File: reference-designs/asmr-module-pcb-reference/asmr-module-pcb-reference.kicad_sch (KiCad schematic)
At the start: 2 parts

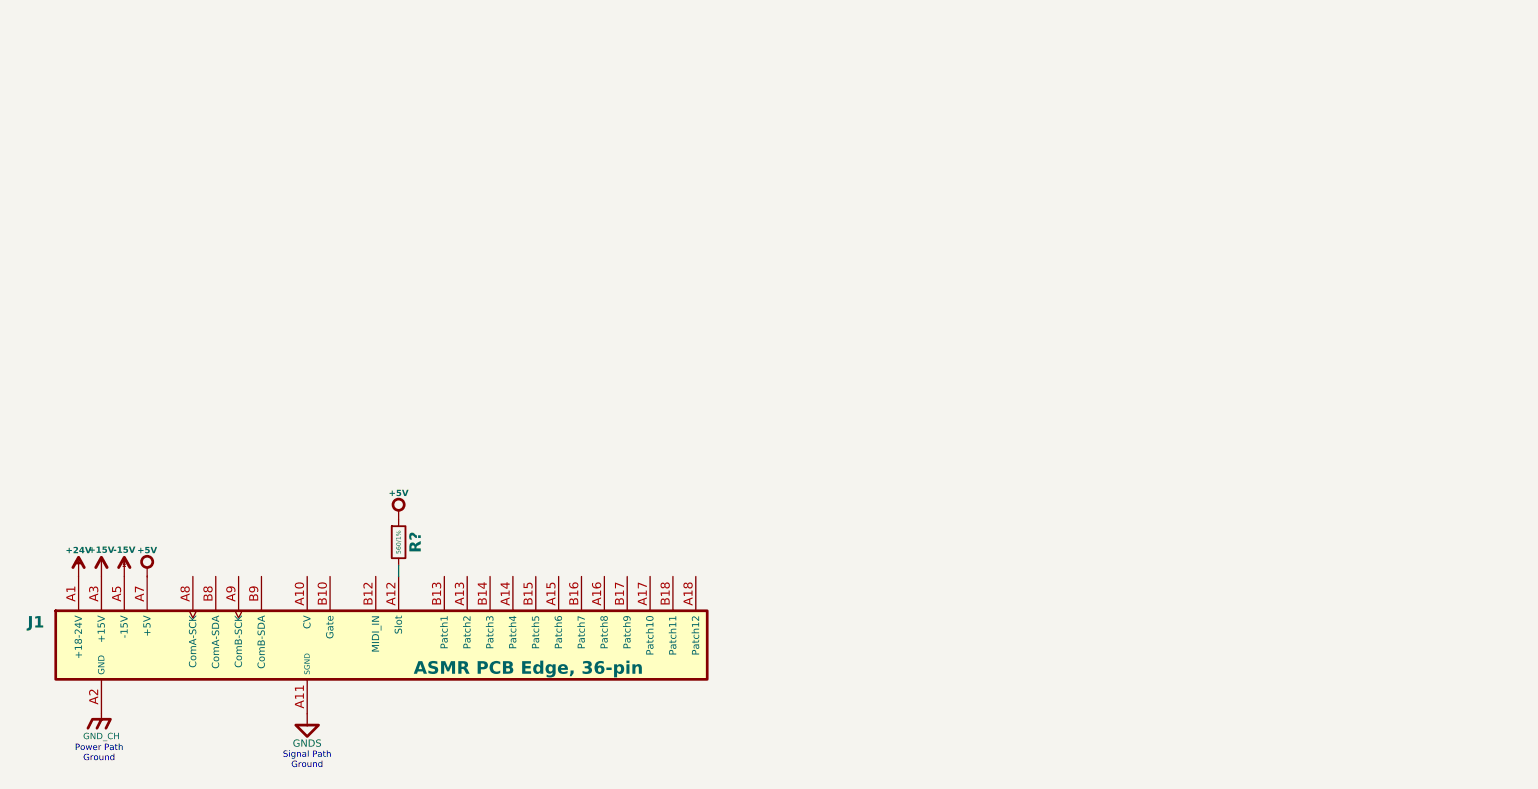
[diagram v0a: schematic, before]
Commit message: Update reference design for 64-pin edge connector.
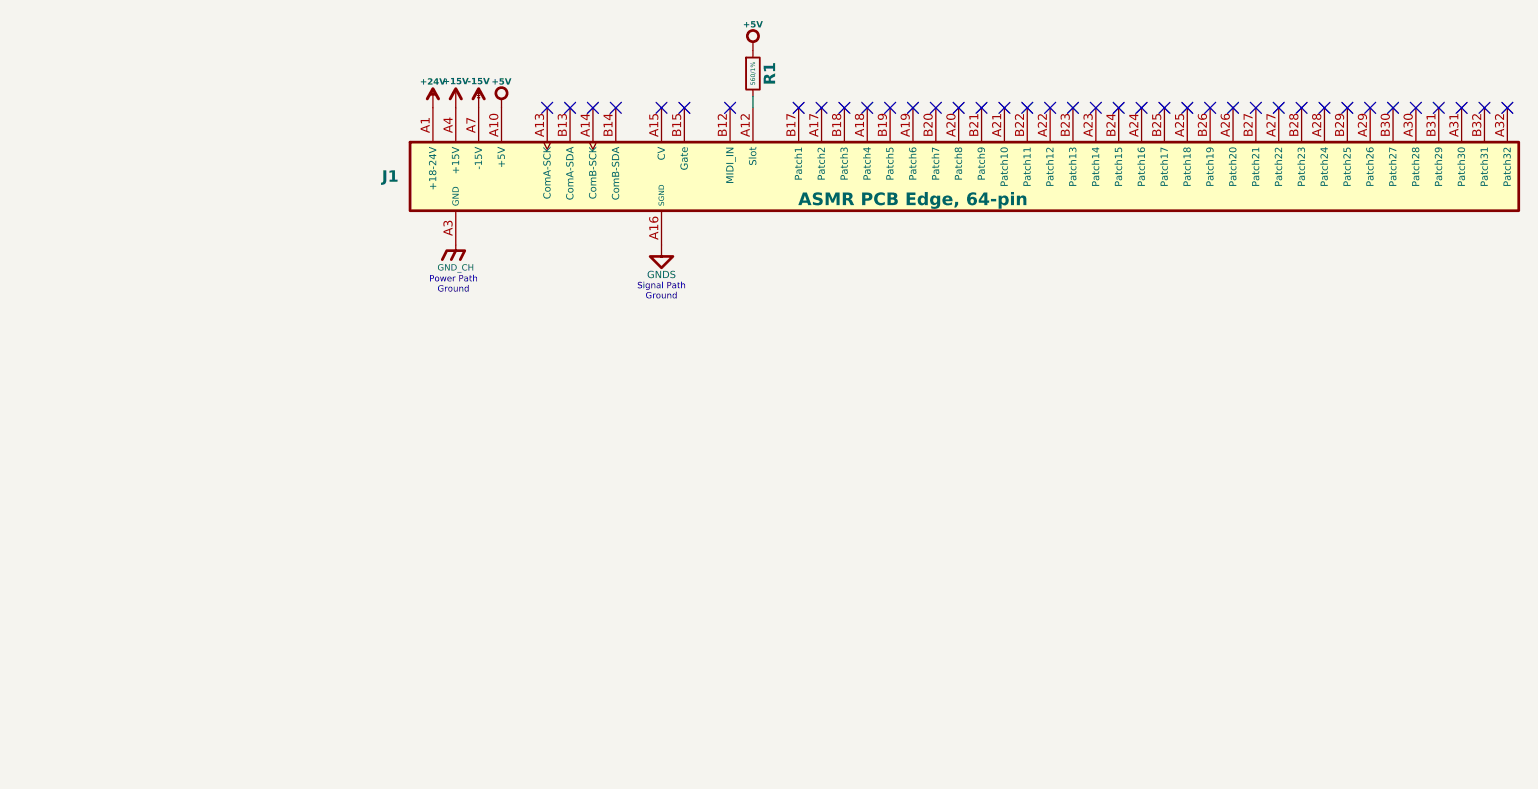
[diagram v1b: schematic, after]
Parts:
- J1: footprint CM_Connector_Edge:ASMR-Edge-36 -> CM_Connector_Edge:ASMR-Edge-64; symbol CM_Connector_Edge:ASMR-36-Edge -> CM_Connector_Edge:ASMR-64-Edge
- R1: renamed from R?; footprint (none) -> CM_Resistor_Capacitor:R_0603_1608Metric
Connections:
- net +15V: now also J1.A4 (+15V), J1.A5 (+15V), J1.B4 (+15V), J1.B5 (+15V); no longer J1.A3 (+15V), J1.B3 (+15V)
- net +24V: now also J1.A2 (+18-24V), J1.B2 (+18-24V)
- net +5V: now also J1.A10 (+5V), J1.A11 (+5V), J1.B10 (+5V), J1.B11 (+5V); no longer J1.A7 (+5V), J1.B7 (+5V)
- net -15V: now also J1.A7 (-15V), J1.A8 (-15V), J1.B7 (-15V), J1.B8 (-15V); no longer J1.A5 (-15V), J1.B5 (-15V)
- net GNDS: now also J1.A16 (SGND), J1.B16 (SGND); no longer J1.A11 (SGND), J1.B11 (SGND)
- net GND_CH: now also J1.A3 (GND), J1.A9 (GND), J1.B3 (GND), J1.B9 (GND); no longer J1.A2 (GND), J1.A4 (GND), J1.B2 (GND), J1.B4 (GND)
- no-connect marks 0 -> 39
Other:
- moved on the sheet: R1
